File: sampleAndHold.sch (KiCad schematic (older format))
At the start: 19 parts, among them Q2 2N3904, U2 TL072, U3 LF398, U4 4047

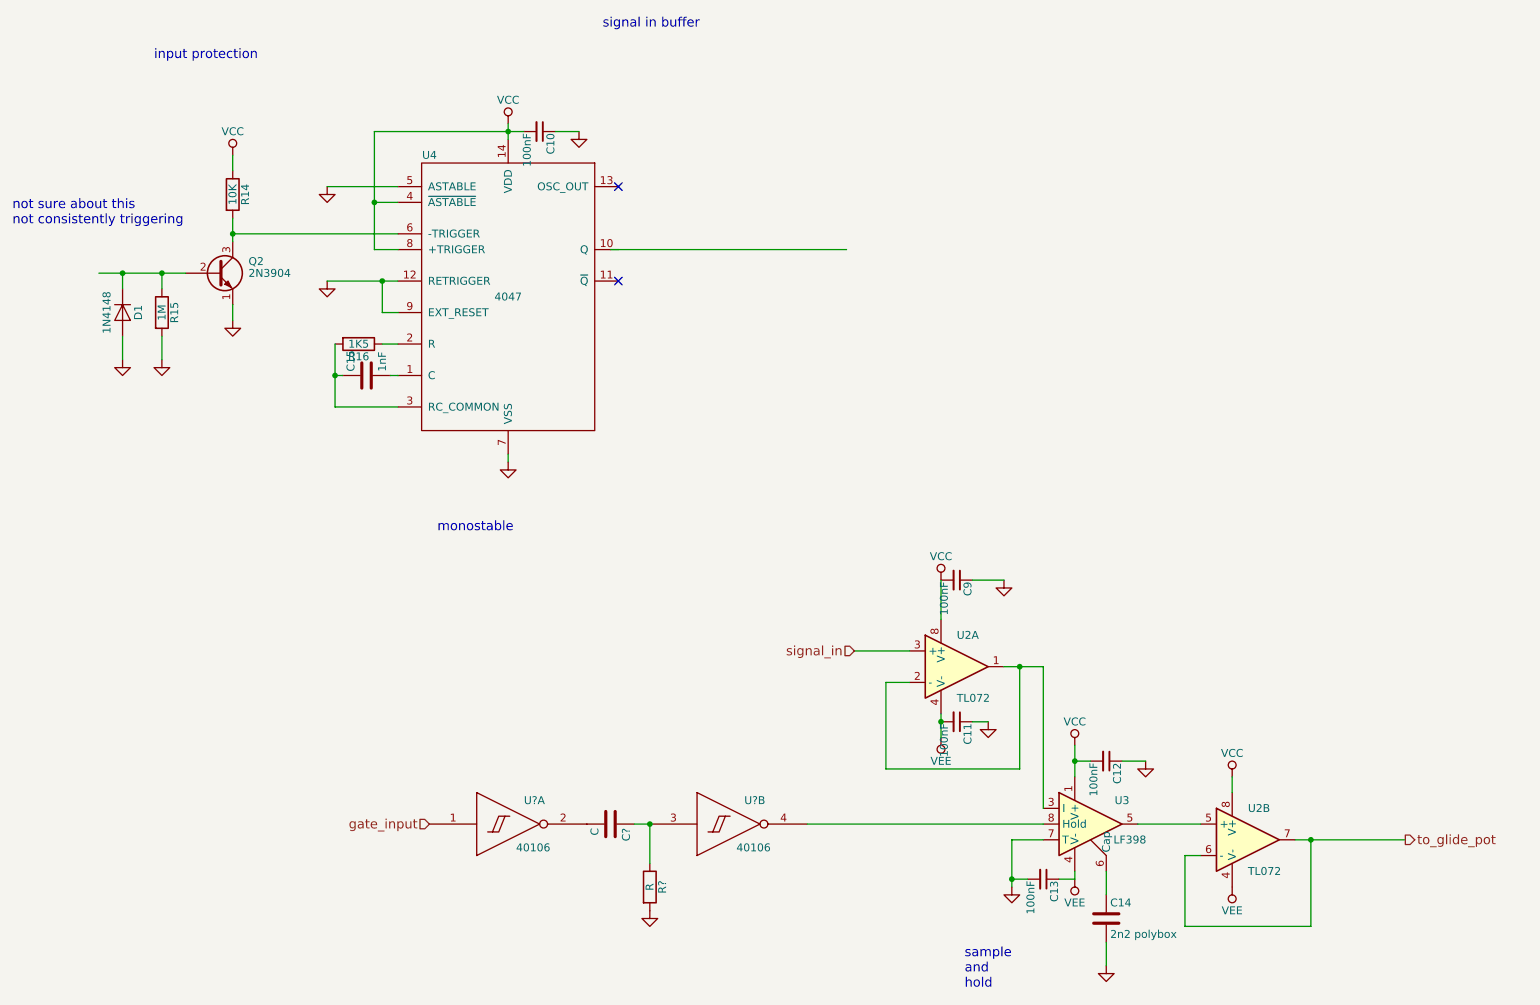
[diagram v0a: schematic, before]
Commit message: changed to 40106 osc and one shot, but input schmitt not working
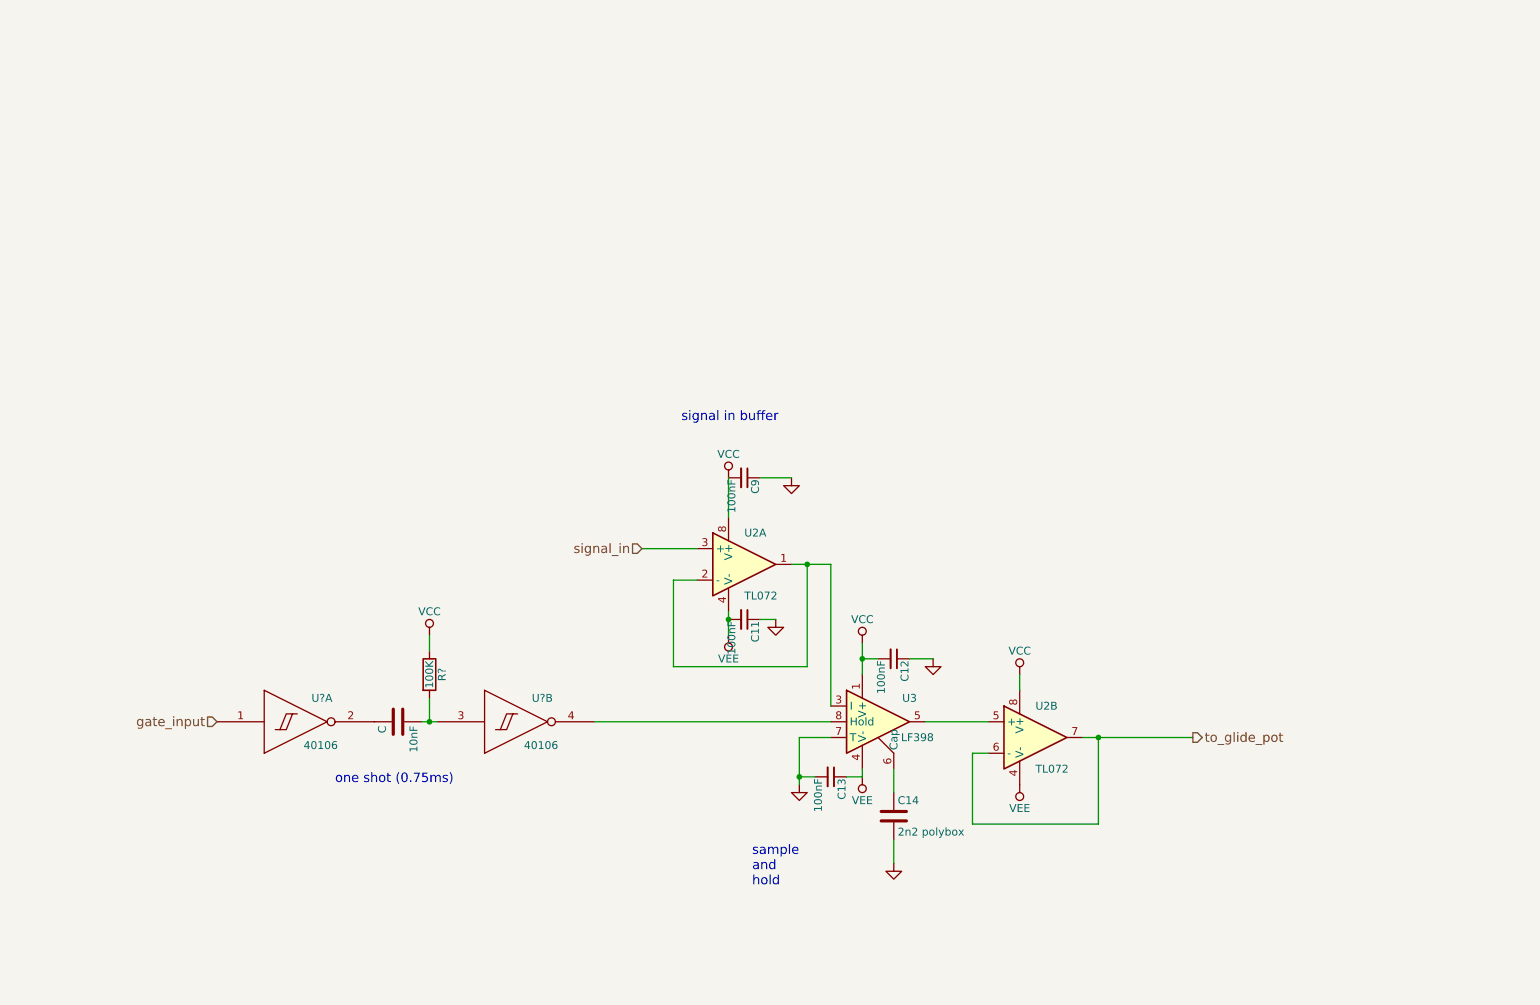
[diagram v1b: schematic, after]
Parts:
- removed C10: 100nF, Capacitors_THT:C_Disc_D3.0mm_W2.0mm_P2.50mm, symbol C_Small
- removed C15: 1nF, Capacitors_THT:C_Rect_L7.2mm_W2.5mm_P5.00mm_FKS2_FKP2_MKS2_MKP2, symbol C
- removed D1: 1N4148, Diodes_THT:D_DO-41_SOD81_P7.62mm_Horizontal, symbol D
- removed Q2: 2N3904, TO_SOT_Packages_THT:TO-92_Molded_Narrow, symbol 2N3904
- removed R14: 10K, Resistors_THT:R_Axial_DIN0204_L3.6mm_D1.6mm_P7.62mm_Horizontal, symbol R
- removed R15: 1M, Resistors_THT:R_Axial_DIN0204_L3.6mm_D1.6mm_P7.62mm_Horizontal, symbol R
- removed R16: 1K5, Resistors_THT:R_Axial_DIN0204_L3.6mm_D1.6mm_P7.62mm_Horizontal, symbol R
- removed U4: 4047, Housings_DIP:DIP-14_W7.62mm_LongPads, symbol 4047
- R?: value R -> 100K
- gave numbers to parts that had none: 1
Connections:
- wire segments 58 -> 33
- no-connect marks 2 -> 0
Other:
- note added: "one shot (0.75ms)"
- note removed: "input protection"
- note removed: "monostable"
- note removed: "not sure about this\nnot consistently triggering"
- moved on the sheet: 10nF, C11, C12, C13, C14, C9, R?, U2A, U2B, U3, U?A, U?B
